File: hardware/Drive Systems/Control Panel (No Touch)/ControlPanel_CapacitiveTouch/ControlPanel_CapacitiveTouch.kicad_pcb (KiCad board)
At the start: 4 copper layers, 50.2 x 30.5 mm, 27 parts, among them J1 Conn_01x03_Pin, J2 Conn_01x03_Pin, J3 Conn_01x03_Pin, J4 Adafruit TPS61040, J5 5v Power Input, J6 Conn_01x02_Pin, J7 Conn_01x02_Pin, J8 Conn_01x02_Pin, Q1 2N7002, Q2 2N7002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

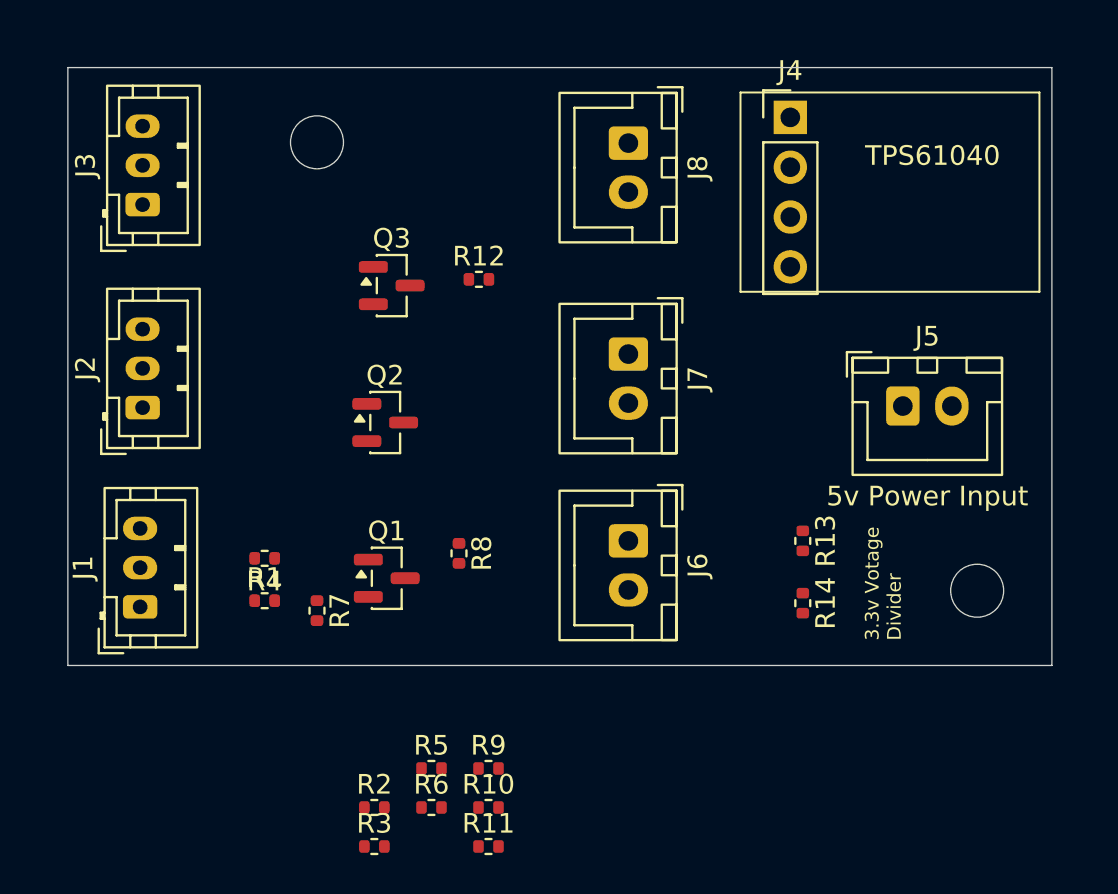
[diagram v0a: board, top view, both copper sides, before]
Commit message: more capacitive touch pcb changes
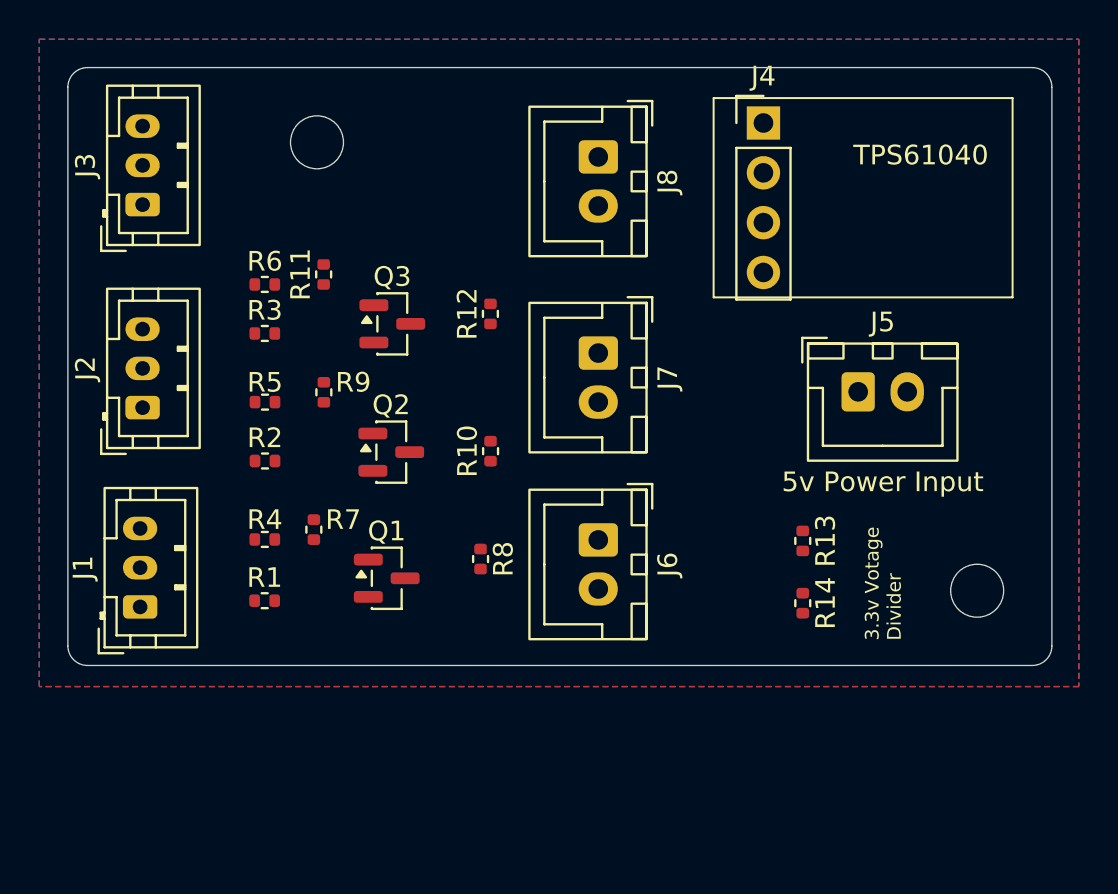
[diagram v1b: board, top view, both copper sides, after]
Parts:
- moved R11 30.4 mm to (137.5, 78.5), turned to 90 degrees
- moved R6 28.0 mm to (134.5, 79.0)
- moved R3 26.7 mm to (134.5, 81.5)
- moved R9 20.9 mm to (137.5, 84.5), turned to 90 degrees
- moved R5 20.5 mm to (134.5, 85.0), turned to 180 degrees
- moved R2 18.5 mm to (134.5, 88.0)
- moved R10 18.2 mm to (146.0, 87.5), turned to 90 degrees
- moved R7 4.13 mm to (137.0, 91.5), turned to 90 degrees
- moved J5 2.39 mm to (164.8, 84.5)
- moved Q3 1.95 mm to (141.0, 81.0)
- moved R12 1.85 mm to (146.0, 80.5), turned to 90 degrees
- moved J8 1.69 mm to (151.5, 72.5)
- moved Q2 1.54 mm to (140.9, 87.5)
- moved J6 1.54 mm to (151.5, 92.0)
- moved J7 1.54 mm to (151.5, 82.5)
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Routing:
- added copper zone on In2.Cu, net +12V
- added copper zone on In2.Cu, net +3.3V
- added copper zone on In2.Cu, net +5V
- added copper zone on B.Cu, net GND
- added copper zone on F.Cu, net GND
- added copper zone on In1.Cu, net GND
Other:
- outline, holes or cut-outs redrawn

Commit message: final v1 pcb for capacitive touch
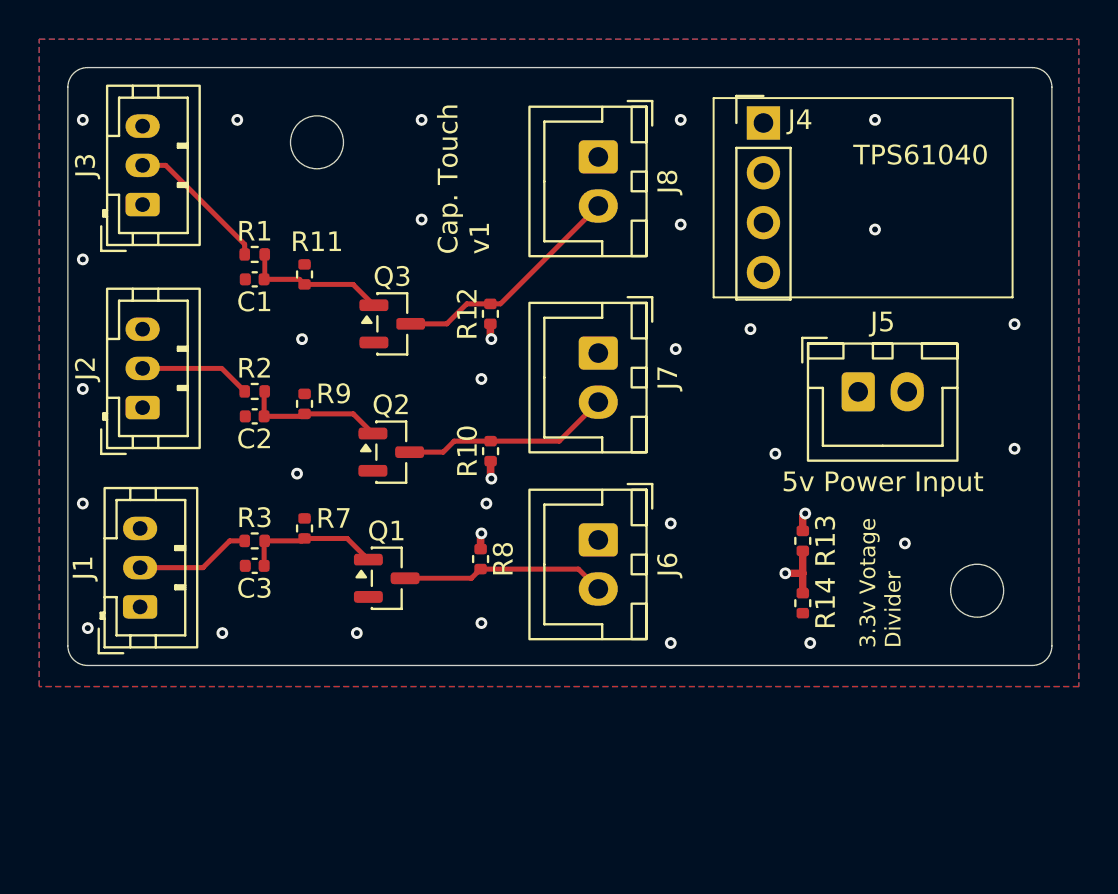
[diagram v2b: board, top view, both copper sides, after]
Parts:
- removed R4, R5, R6: 330, Resistor_SMD:R_0402_1005Metric
- added C1: 100n, Capacitor_SMD:C_0402_1005Metric, F.Cu at (134.0, 78.7)
- added C2: 100n, Capacitor_SMD:C_0402_1005Metric, F.Cu at (134.0, 85.7)
- added C3: 100n, Capacitor_SMD:C_0402_1005Metric, F.Cu at (134.0, 93.3)
- R13: value 1k -> 10k
- R14: value 2k -> 20k
- moved R1 17.7 mm to (134.0, 77.5)
- moved R3 10.6 mm to (134.0, 92.1)
- moved R2 3.58 mm to (134.0, 84.5)
- moved R9 1.15 mm to (136.5, 85.1)
- moved R11 0.97 mm to (136.5, 78.5)
- moved R7 0.48 mm to (136.5, 91.4)
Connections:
- net CENTER renamed Net-(Q2-G)
- Q1 pad 1: LEFT -> Net-(Q1-G)
- Q3 pad 1: RIGHT -> Net-(Q3-G)
- R1 pad 1: LEFT_SIGNAL_12V -> RIGHT_SIGNAL_12V
- R1 pad 2: LEFT -> Net-(Q3-G)
- R11 pad 1: RIGHT -> Net-(Q3-G)
- R3 pad 1: RIGHT_SIGNAL_12V -> LEFT_SIGNAL_12V
- R3 pad 2: RIGHT -> Net-(Q1-G)
- R7 pad 1: LEFT -> Net-(Q1-G)
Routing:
- net RIGHT_ACTIVE_LOW: track 0.00 -> 12.1 mm
- net CENTER_ACTIVE_LOW: track 0.00 -> 10.7 mm
- net LEFT_ACTIVE_LOW: track 0.00 -> 10.5 mm
- net Net-(Q3-G): track 0.00 -> 7.43 mm
- net RIGHT_SIGNAL_12V: track 0.00 -> 7.38 mm
- net Net-(Q2-G): track 0.00 -> 7.29 mm
- net Net-(Q1-G): track 0.00 -> 7.07 mm
- net LEFT_SIGNAL_12V: track 0.00 -> 5.90 mm
- net CENTER_SIGNAL_12V: track 0.00 -> 5.69 mm
- net +3.3V: track 0.00 -> 5.56 mm, vias 0 -> 4
- net +5V: track 0.00 -> 0.94 mm, vias 0 -> 1
- net GND: vias 0 -> 28
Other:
- board text added: "Cap. Touch v1"
- board text added: "Capactive Touch 12v Adapter v1"
